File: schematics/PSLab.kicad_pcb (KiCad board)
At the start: 4 copper layers, 99 x 53.3 mm, 181 parts, among them J1 DoublePins, J11 Li-Ion Battery, J2 Power Pins, J3 Wave Generator, J4 I2C, J5 I2C, J6 ESP01, J7 UART, J8 Battery Switch, J9 SPI, P1 SDCard, Q1 MMBT3906, Q2 MMBT3904, Q3 MMBT3906, SW1 BOOT, SW2 MCLR Reset, SW3 USB_C - Generic, U1 FP6291, U10 TL082, U11 TL082, U12 MCP4728, U13 MCP6S21, U14 MCP6S21, U15 CP2102N-xxx-xQFN20x, U16 SP0503BAHT, U17 IP5189T, U2 74HC126, U3 PIC24EP256GP204, U4 DS1307Z+, U5 TP7660H, U6 HT7333-A, U7 LM324, U8 TL082, U9 TL082, X2 32.768 kHz, Y1 12 MHz

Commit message: Temp6
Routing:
- net +3V3: track 243.9 -> 241.0 mm
- net SDA: track 80.4 -> 82.2 mm
- net GND: track 241.2 -> 240.7 mm, vias 144 -> 153

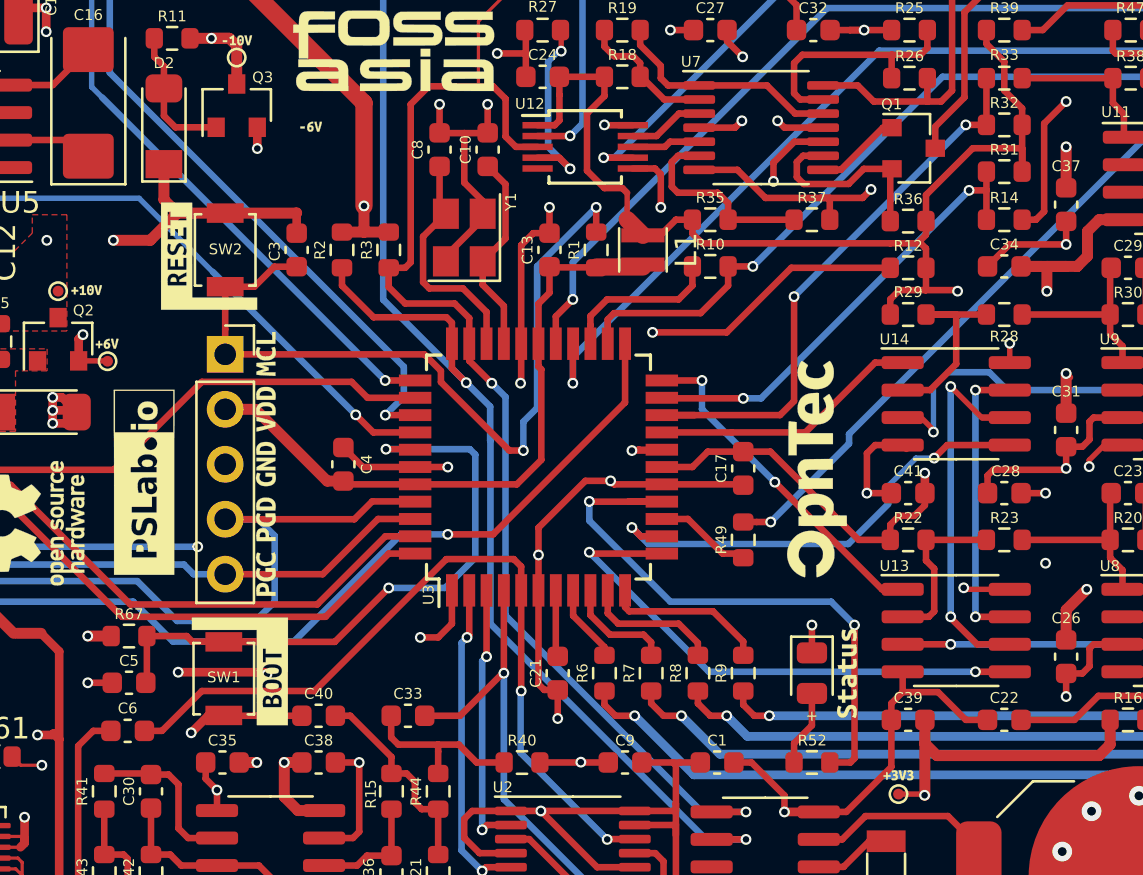
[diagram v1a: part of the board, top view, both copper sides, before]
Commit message: refactor: fix all warnings, replace SW1 and SW2, before gerber generation
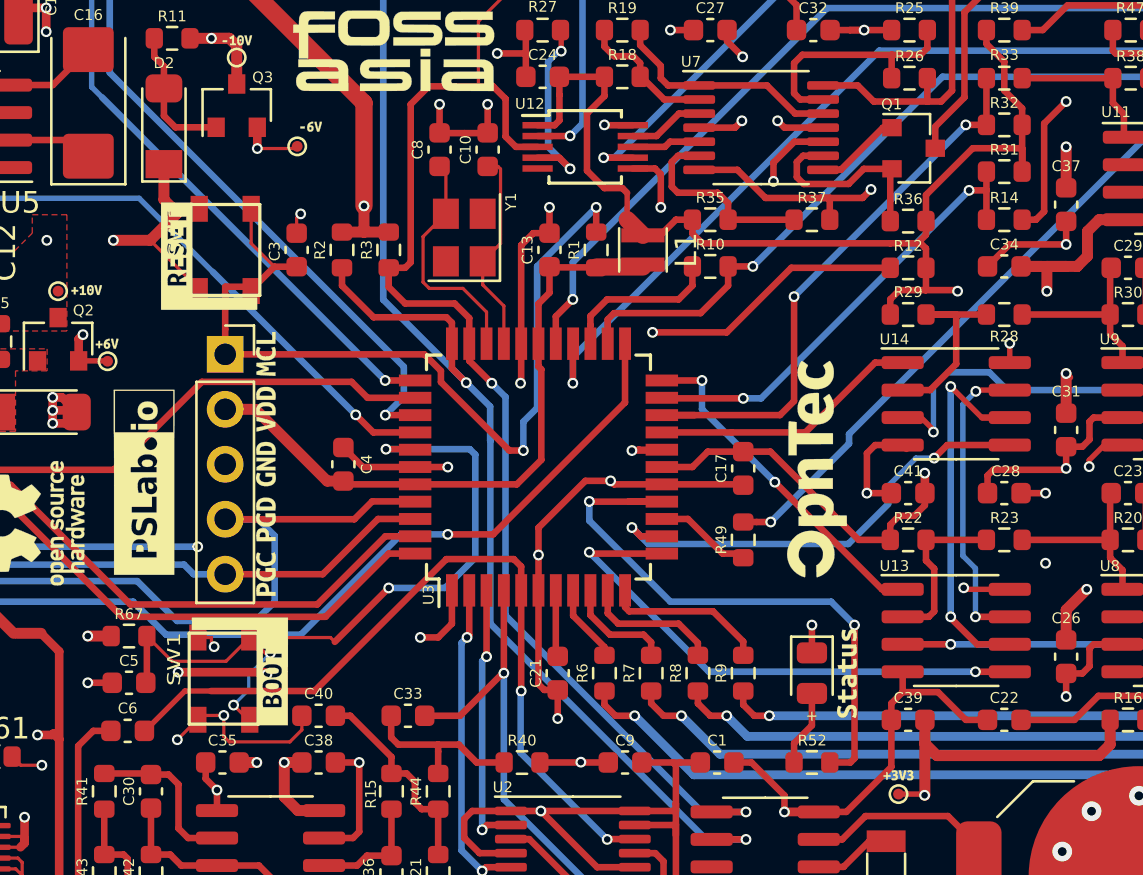
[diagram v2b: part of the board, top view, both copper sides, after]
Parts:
- added TP3: TEST, PSLab:Voltage_Test_Point, F.Cu at (136.9, 73.0)
- C10, C8: value 33pF -> 12pF
- SW1: value BOOT -> SW_MEC_5E; footprint Button_Switch_SMD:SW_SPST_B3U-1000P -> PSLab:button_SPST_3x4x2.5
- SW2: value MCLR Reset -> SW_MEC_5E; footprint Button_Switch_SMD:SW_SPST_B3U-1000P -> PSLab:button_SPST_3x4x2.5
- turned SW2 to 270 degrees
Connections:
- D5 pad 2: (no net) -> Net-(D5-Pad2)
- J6 pad 3: (no net) -> Net-(J6-Pad3)
- J6 pad 5: (no net) -> Net-(J6-Pad5)
- J6 pad 6: (no net) -> Net-(J6-Pad6)
- P1 pad 1: (no net) -> Net-(P1-Pad1)
- P1 pad 10: (no net) -> Net-(P1-Pad10)
- P1 pad 8: (no net) -> Net-(P1-Pad8)
- P1 pad 9: (no net) -> Net-(P1-Pad9)
- SW1 pad 2: GND -> BOOT
- SW2 pad 2: GND -> MCLR
- SW3 pad A8: (no net) -> Net-(SW3-PadA8)
- SW3 pad B8: (no net) -> Net-(SW3-PadB8)
- U12 pad 5: (no net) -> Net-(U12-Pad5)
- U15 pad 1: (no net) -> Net-(U15-Pad1)
- U15 pad 10: (no net) -> Net-(U15-Pad10)
- U15 pad 11: (no net) -> Net-(U15-Pad11)
- U15 pad 13: (no net) -> Net-(U15-Pad13)
- U15 pad 14: (no net) -> Net-(U15-Pad14)
- U15 pad 15: (no net) -> Net-(U15-Pad15)
- U15 pad 16: (no net) -> Net-(U15-Pad16)
- U15 pad 19: (no net) -> Net-(U15-Pad19)
- U15 pad 2: (no net) -> Net-(U15-Pad2)
- U15 pad 20: (no net) -> Net-(U15-Pad20)
- U17 pad 1: (no net) -> Net-(U17-Pad1)
- U17 pad 10: (no net) -> Net-(U17-Pad10)
- U17 pad 18: (no net) -> Net-(U17-Pad18)
- U17 pad 19: (no net) -> Net-(U17-Pad19)
- U17 pad 2: (no net) -> Net-(U17-Pad2)
- U17 pad 22: (no net) -> Net-(U17-Pad22)
- U17 pad 23: (no net) -> Net-(U17-Pad23)
- U17 pad 24: (no net) -> Net-(U17-Pad24)
- U17 pad 5: (no net) -> Net-(U17-Pad5)
- U17 pad 6: (no net) -> Net-(U17-Pad6)
- U17 pad 8: (no net) -> Net-(U17-Pad8)
- U4 pad 7: (no net) -> Net-(U4-Pad7)
- U5 pad 1: (no net) -> Net-(U5-Pad1)
- U5 pad 6: (no net) -> Net-(U5-Pad6)
- U5 pad 7: (no net) -> Net-(U5-Pad7)
- Y1 pad 2: GND -> Net-(Y1-Pad2)
- Y1 pad 4: GND -> Net-(Y1-Pad4)
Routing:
- net BOOT: track 30.9 -> 35.7 mm, vias 2 -> 4
- net GND: track 240.7 -> 236.5 mm, vias 153 -> 156
- net MCLR: track 44.1 -> 47.3 mm
- net -6V: track 89.7 -> 91.6 mm
- net CS.CH3: track 42.8 -> 41.0 mm

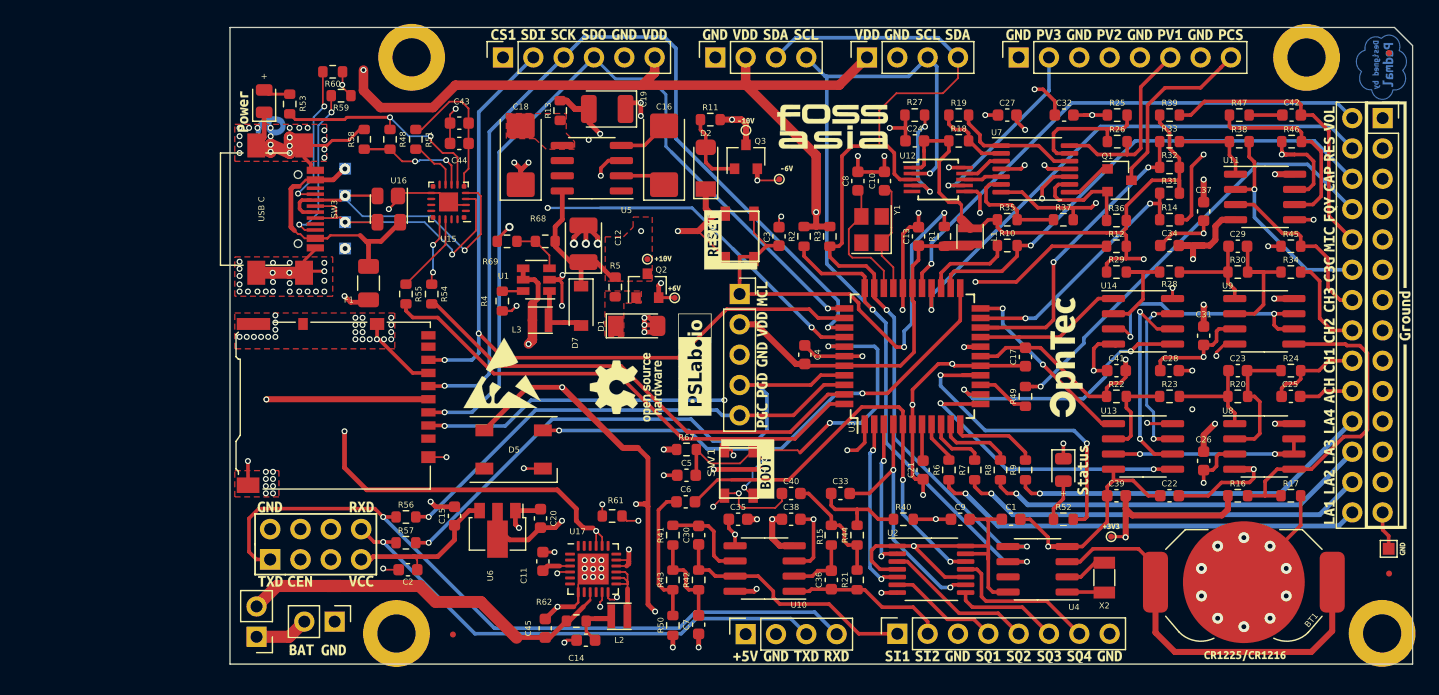
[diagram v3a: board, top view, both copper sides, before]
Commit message: Add battery socket and SW3 in PCB
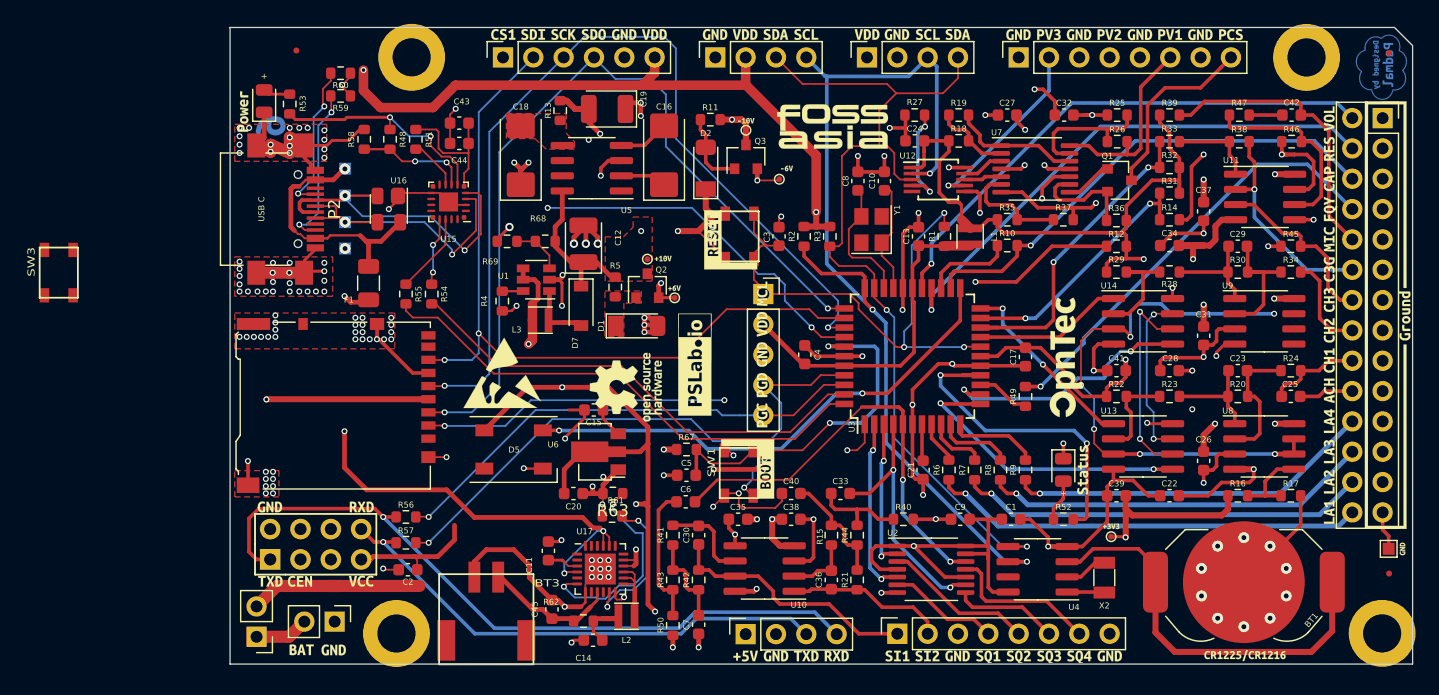
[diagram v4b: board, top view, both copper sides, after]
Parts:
- added BT3: Battery_Cell, PSLab:2.0mm_connector_edge, F.Cu at (112.4, 107.6)
- added P2: USB_C - Generic, incremental_library:USB_C_Receptacle_12pin_SMT, F.Cu at (94.0, 75.5)
- added R63: 51k, Resistor_SMD:R_0603_1608Metric, F.Cu at (123.0, 99.3)
- SW3: value USB_C - Generic -> SW_MEC_5E; footprint incremental_library:USB_C_Receptacle_12pin_SMT -> PSLab:button_SPST_3x4x2.5
- moved FID1 50.6 mm to (96.5, 62.2)
- moved SW3 18.2 mm to (76.6, 80.8)
- moved C15 14.7 mm to (121.4, 92.3), turned to 0 degrees
- moved U6 10.7 mm to (121.8, 95.8), turned to 180 degrees
- moved C20 3.46 mm to (119.7, 99.3), turned to 180 degrees
- moved Z1 1.99 mm to (135.6, 82.6)
- moved C45 1.68 mm to (117.9, 109.0)
- moved C11 0.99 mm to (117.6, 104.1)
- moved R60 0.67 mm to (100.2, 64.1)
- moved C14 0.60 mm to (121.3, 111.6)
- moved R62 0.60 mm to (120.5, 110.0)
- moved U17 0.60 mm to (122.0, 105.6)
- moved L2 0.60 mm to (124.1, 109.6)
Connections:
- D5 pad 2: Net-(D5-Pad2) -> (no net)
- J6 pad 3: Net-(J6-Pad3) -> (no net)
- J6 pad 5: Net-(J6-Pad5) -> (no net)
- J6 pad 6: Net-(J6-Pad6) -> (no net)
- P1 pad 1: Net-(P1-Pad1) -> (no net)
- P1 pad 10: Net-(P1-Pad10) -> (no net)
- P1 pad 8: Net-(P1-Pad8) -> (no net)
- P1 pad 9: Net-(P1-Pad9) -> (no net)
- R16 pad 1: /OSC_REF -> Net-(R16-Pad1)
- R17 pad 1: /OSC_REF -> Net-(R16-Pad1)
- U12 pad 5: Net-(U12-Pad5) -> (no net)
- U13 pad 3: Net-(U13-Pad3) -> /OSC_REF
- U14 pad 3: Net-(U14-Pad3) -> /OSC_REF
- U15 pad 1: Net-(U15-Pad1) -> (no net)
- U15 pad 10: Net-(U15-Pad10) -> (no net)
- U15 pad 11: Net-(U15-Pad11) -> (no net)
- U15 pad 13: Net-(U15-Pad13) -> (no net)
- U15 pad 14: Net-(U15-Pad14) -> (no net)
- U15 pad 15: Net-(U15-Pad15) -> (no net)
- U15 pad 16: Net-(U15-Pad16) -> (no net)
- U15 pad 19: Net-(U15-Pad19) -> (no net)
- U15 pad 2: Net-(U15-Pad2) -> (no net)
- U15 pad 20: Net-(U15-Pad20) -> (no net)
- U17 pad 1: Net-(U17-Pad1) -> (no net)
- U17 pad 10: Net-(U17-Pad10) -> (no net)
- U17 pad 18: Net-(U17-Pad18) -> (no net)
- U17 pad 19: Net-(U17-Pad19) -> (no net)
- U17 pad 2: Net-(U17-Pad2) -> (no net)
- U17 pad 22: Net-(U17-Pad22) -> (no net)
- U17 pad 23: Net-(U17-Pad23) -> (no net)
- U17 pad 24: Net-(U17-Pad24) -> (no net)
- U17 pad 5: Net-(U17-Pad5) -> (no net)
- U17 pad 8: Net-(U17-Pad8) -> Net-(SW3-Pad3)
- U4 pad 7: Net-(U4-Pad7) -> (no net)
- U5 pad 1: Net-(U5-Pad1) -> (no net)
- U5 pad 6: Net-(U5-Pad6) -> (no net)
- U5 pad 7: Net-(U5-Pad7) -> (no net)
- U8 pad 5: /OSC_REF -> Net-(R16-Pad1)
- U8 pad 6: Net-(U13-Pad3) -> /OSC_REF
- U8 pad 7: Net-(U13-Pad3) -> /OSC_REF
- U9 pad 5: /OSC_REF -> (no net)
- U9 pad 6: Net-(U14-Pad3) -> (no net)
- U9 pad 7: Net-(U14-Pad3) -> (no net)
- Y1 pad 2: Net-(Y1-Pad2) -> (no net)
- Y1 pad 4: Net-(Y1-Pad4) -> (no net)
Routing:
- net Net-(U14-Pad3): track 20.0 -> 0.00 mm, vias 2 -> 0
- net /OSC_REF: track 27.3 -> 46.6 mm, vias 0 -> 6
- net Net-(R63-Pad1): track 0.00 -> 17.6 mm, vias 0 -> 2
- net Net-(U13-Pad3): track 16.8 -> 0.00 mm, vias 2 -> 0
- net GND: track 236.5 -> 251.6 mm, vias 156 -> 154
- net /BAT+: track 34.1 -> 27.2 mm
- net Net-(R16-Pad1): track 0.00 -> 6.83 mm
- net SDA: track 82.2 -> 77.0 mm
- net MCLR: track 47.3 -> 43.4 mm
- net +3V3: track 241.0 -> 237.7 mm
- net SQR4_: track 36.4 -> 39.1 mm
- net PGD2: track 49.6 -> 47.5 mm
- net +5V: track 171.3 -> 169.2 mm, vias 9 -> 8
- net /CP2102_Vreg: track 12.3 -> 11.5 mm
- net SPI.CS: track 48.0 -> 48.8 mm

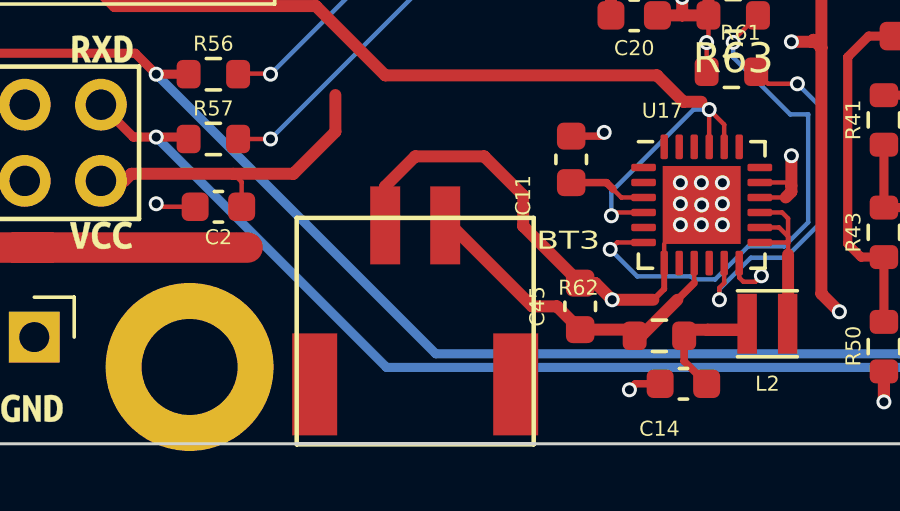
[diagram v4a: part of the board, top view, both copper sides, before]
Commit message: refactor: replace PGA MAX6S@! with TL082 and MAX5400, modify PCB
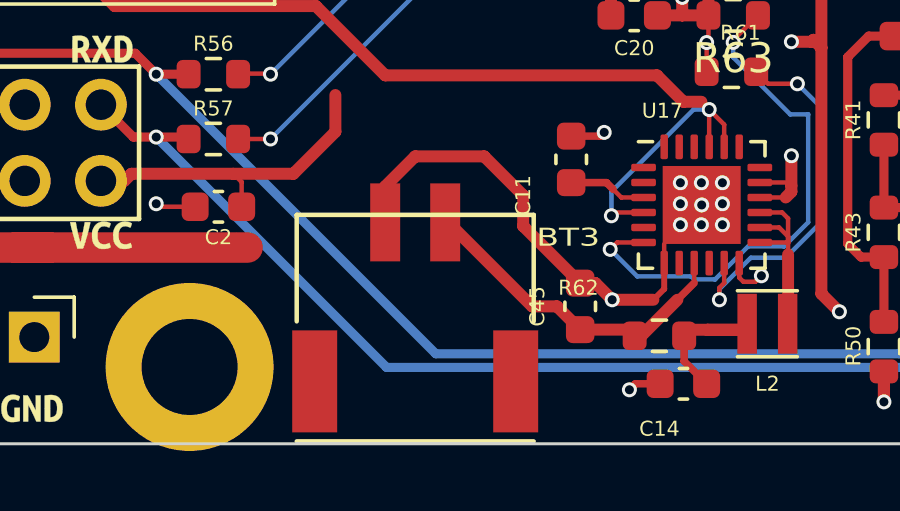
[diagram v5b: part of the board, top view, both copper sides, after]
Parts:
- moved BT3 0.10 mm to (112.4, 107.5)
